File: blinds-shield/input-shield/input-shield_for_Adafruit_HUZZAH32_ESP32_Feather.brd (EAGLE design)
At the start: 50.8 x 22.9 mm, 18 parts

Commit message: Routing attempts
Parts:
- moved R2_BTN1_PULLDOWN 11.9 mm to (33.0, 7.43), turned to 180 degrees
- moved R6_PR2 6.62 mm to (12.3, 6.22), turned to 180 degrees
- moved R4_BTN3_PULLDOWN 4.24 mm to (27.9, 14.0), turned to 180 degrees
- moved R3_BTN2_PULLDOWN 3.80 mm to (30.5, 10.5), turned to 180 degrees
- moved R5_PR1 1.74 mm to (12.3, 10.2), turned to 180 degrees
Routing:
- net 3.3V: track 0.00 -> 54.6 mm
- net IO33_A9: track 0.00 -> 35.0 mm
- net IO32_A7: track 0.00 -> 34.7 mm
- net IO15_A8: track 0.00 -> 32.9 mm
- net N$1: track 0.00 -> 15.2 mm
- net IO27_A10: track 0.00 -> 5.42 mm

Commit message: Add files via upload
nu shieeeld
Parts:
- removed U$34, U$35: FIDUCIAL_1MM, microbuilder:FIDUCIAL_1MM
- added R_DUMMY_PR1, R_DUMMY_PR2: 0k ohm, rcl:0204/7
- moved R6_PR2 1.06 mm to (12.6, 5.21)
- moved R5_PR1 0.46 mm to (12.7, 10.4)
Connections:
- new net N$4: R5_PR1.2, R_DUMMY_PR1.1
- new net N$5: R6_PR2.2, R_DUMMY_PR2.1
- net N$2: now also R_DUMMY_PR1.2; no longer R5_PR1.2
- net N$3: now also R_DUMMY_PR2.2; no longer R6_PR2.2
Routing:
- net GND: track 0.00 -> 42.5 mm
- net 3.3V: track 54.6 -> 82.8 mm
- net IO15_A8: track 32.9 -> 21.6 mm
- net IO33_A9: track 35.0 -> 25.7 mm
- net N$5: track 0.00 -> 8.81 mm
- net N$4: track 0.00 -> 8.72 mm
- net IO32_A7: track 34.7 -> 28.8 mm
- net N$2: track 0.00 -> 3.87 mm
- net N$3: track 0.00 -> 3.23 mm
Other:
- board size 50.8 x 22.9 mm -> 52.6 x 25 mm

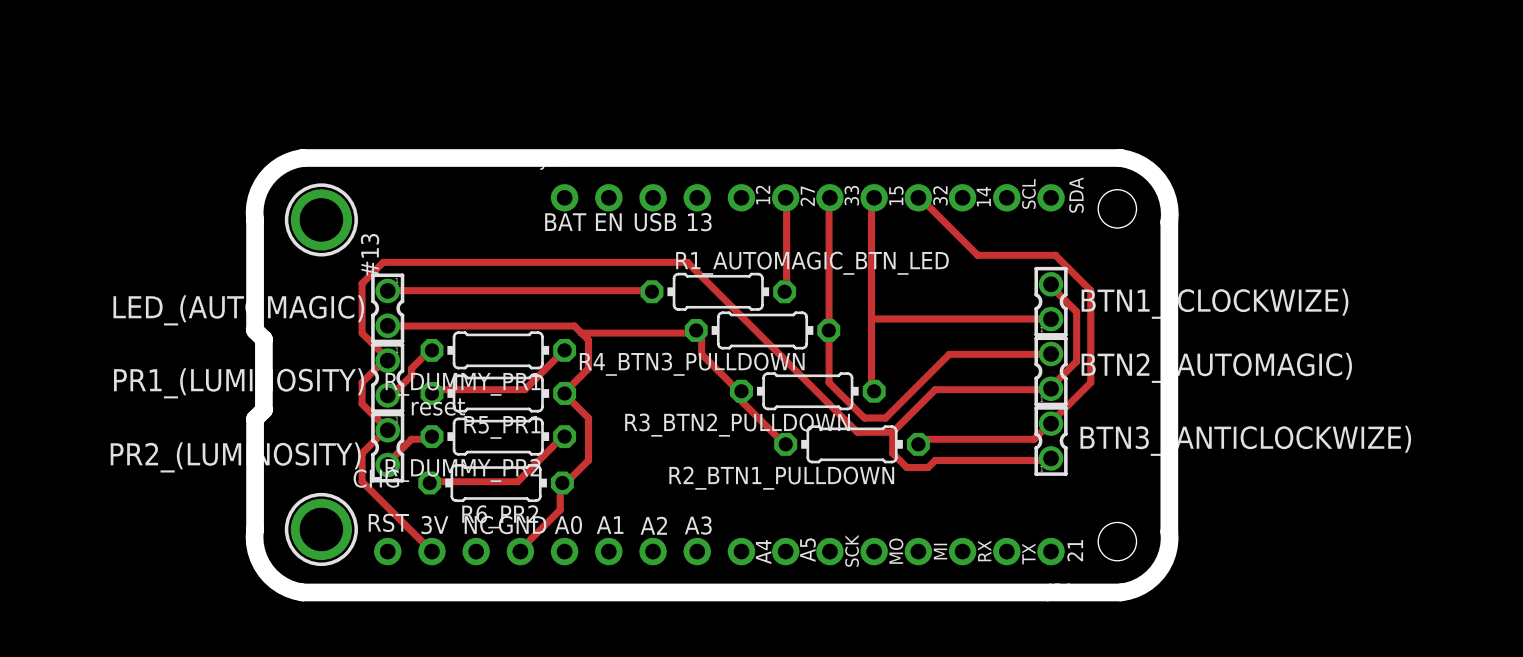
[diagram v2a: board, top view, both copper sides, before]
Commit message: Add files via upload
A0 and A1 are now connected to photoresistors.
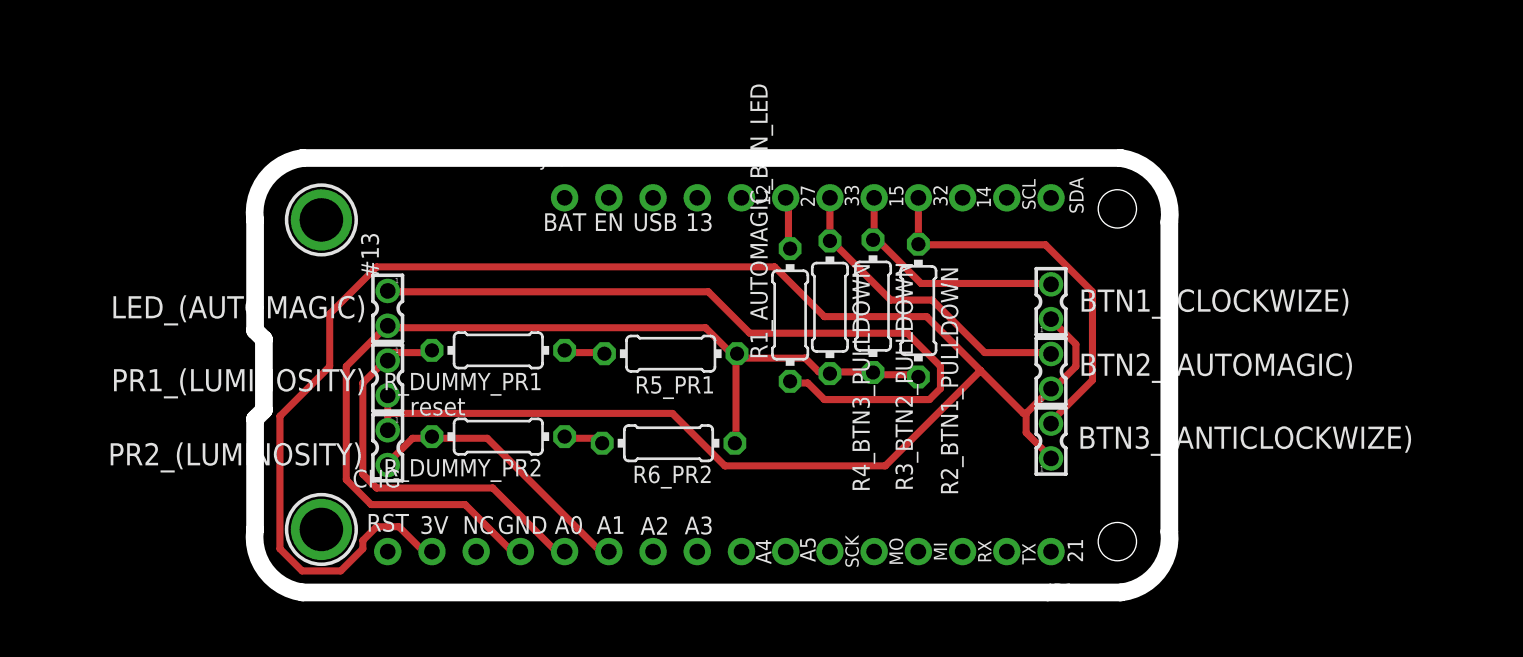
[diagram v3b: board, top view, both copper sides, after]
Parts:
- moved R5_PR1 10.2 mm to (22.6, 12.6)
- moved R6_PR2 10.2 mm to (22.5, 7.49)
- moved R2_BTN1_PULLDOWN 8.58 mm to (36.8, 15.1), turned to 270 degrees
- moved R3_BTN2_PULLDOWN 6.16 mm to (34.2, 15.4), turned to 270 degrees
- moved R1_AUTOMAGIC_BTN_LED 4.34 mm to (29.5, 14.9), turned to 90 degrees
- moved R4_BTN3_PULLDOWN 4.10 mm to (31.8, 15.3), turned to 270 degrees
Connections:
- removed net N$2: PR1_(LUMINOSITY).2, R_DUMMY_PR1.2
- removed net N$3: PR2_(LUMINOSITY).2, R_DUMMY_PR2.2
- net 3.3V: now also BTN1_(CLOCKWIZE).1, PR1_(LUMINOSITY).2; no longer BTN1_(CLOCKWIZE).2, PR1_(LUMINOSITY).1
- net A0_DAC2: now also PR1_(LUMINOSITY).1, R_DUMMY_PR1.2
- net A1_DAC1: now also PR2_(LUMINOSITY).2, R_DUMMY_PR2.2
- net IO15_A8: now also BTN1_(CLOCKWIZE).2; no longer BTN1_(CLOCKWIZE).1
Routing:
- net 3.3V: track 82.8 -> 120.5 mm
- net N$1: track 15.2 -> 44.2 mm
- net A0_DAC2: track 0.00 -> 23.6 mm
- net GND: track 42.5 -> 58.8 mm
- net A1_DAC1: track 0.00 -> 16.2 mm
- net IO33_A9: track 25.7 -> 17.9 mm
- net IO15_A8: track 21.6 -> 13.8 mm
- net IO32_A7: track 28.8 -> 22.3 mm
- net N$5: track 8.81 -> 2.38 mm
- net N$4: track 8.72 -> 2.44 mm
- net N$2: track 3.87 -> 0.00 mm
- net N$3: track 3.23 -> 0.00 mm
- net IO27_A10: track 5.49 -> 3.04 mm

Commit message: Add files via upload
Moved some lines.
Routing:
- net GND: track 58.8 -> 60.0 mm
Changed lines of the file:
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@@
 <setting verticaltext="up"/>
 </settings>
-<grid distance="30" unitdist="mil" unit="mil" style="lines" multiple="1" display="yes" altdistance="0.025" altunitdist="inch" altunit="mil"/>
+<grid distance="0.000123031496" unitdist="mil" unit="mil" style="lines" multiple="1" display="no" altdistance="0.000123031496" altunitdist="mil" altunit="mil"/>
 <layers>
 <layer number="1" name="Top" color="4" fill="1" visible="yes" active="yes"/>
@@
 <wire x1="26.19375" y1="12.54125" x2="26.416" y2="12.6365" width="0.4064" layer="1"/>
 <wire x1="13.49375" y1="1.27" x2="13.97" y2="1.27" width="0.4064" layer="1"/>
-<wire x1="10.795" y1="3.96875" x2="13.49375" y2="1.27" width="0.4064" layer="1"/>
-<wire x1="5.3975" y1="3.96875" x2="10.795" y2="3.96875" width="0.4064" layer="1"/>
-<wire x1="3.96875" y1="5.3975" x2="5.3975" y2="3.96875" width="0.4064" layer="1"/>
-<wire x1="3.96875" y1="11.90625" x2="3.96875" y2="5.3975" width="0.4064" layer="1"/>
-<wire x1="6.19125" y1="14.12875" x2="3.96875" y2="11.90625" width="0.4064" layer="1"/>
+<wire x1="11.180671875" y1="3.583078125" x2="13.49375" y2="1.27" width="0.4064" layer="1"/>
+<wire x1="5.032475" y1="3.583078125" x2="11.180671875" y2="3.583078125" width="0.4064" layer="1"/>
+<wire x1="2.863878125" y1="5.751675" x2="5.032475" y2="3.583078125" width="0.4064" layer="1"/>
+<wire x1="6.19125" y1="14.12875" x2="4.294490625" y2="12.231990625" width="0.4064" layer="1"/>
+<wire x1="4.294490625" y1="12.231990625" x2="3.831065625" y2="11.1083" width="0.4064" layer="1"/>
+<wire x1="3.831065625" y1="11.1083" x2="2.863878125" y2="9.92700625" width="0.4064" layer="1"/>
+<wire x1="2.863878125" y1="9.92700625" x2="2.863878125" y2="5.751675" width="0.4064" layer="1"/>
 <wire x1="6.19125" y1="14.12875" x2="6.35" y2="14.24" width="0.4064" layer="1"/>
 <wire x1="31.115" y1="11.58875" x2="31.59125" y2="11.58875" width="0.4064" layer="1"/>
@@
 <wire x1="6.35" y1="12.3825" x2="6.35" y2="12.2395" width="0.4064" layer="1"/>
 <wire x1="16.03375" y1="1.27" x2="16.51" y2="1.27" width="0.4064" layer="1"/>
-<wire x1="12.3825" y1="4.92125" x2="16.03375" y2="1.27" width="0.4064" layer="1"/>
-<wire x1="5.715" y1="4.92125" x2="12.3825" y2="4.92125" width="0.4064" layer="1"/>
-<wire x1="4.92125" y1="5.715" x2="5.715" y2="4.92125" width="0.4064" layer="1"/>
-<wire x1="4.92125" y1="10.95375" x2="4.92125" y2="5.715" width="0.4064" layer="1"/>
-<wire x1="6.19125" y1="12.22375" x2="4.92125" y2="10.95375" width="0.4064" layer="1"/>
+<wire x1="12.849365625" y1="4.454384375" x2="16.03375" y2="1.27" width="0.4064" layer="1"/>
+<wire x1="5.41100625" y1="4.454384375" x2="12.849365625" y2="4.454384375" width="0.4064" layer="1"/>
+<wire x1="4.880675" y1="4.984715625" x2="5.41100625" y2="4.454384375" width="0.4064" layer="1"/>
+<wire x1="4.880675" y1="10.913175" x2="4.880675" y2="4.984715625" width="0.4064" layer="1"/>
+<wire x1="6.19125" y1="12.22375" x2="4.880675" y2="10.913175" width="0.4064" layer="1"/>
 <wire x1="6.19125" y1="12.22375" x2="6.35" y2="12.2395" width="0.4064" layer="1"/>
 </signal>
